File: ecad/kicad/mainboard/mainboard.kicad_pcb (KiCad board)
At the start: 2 copper layers, 99.1 x 81.3 mm, 34 parts, among them IC1 74HC86, J1 SENSORS, J2 CONN_06SILK_FEMALE_PTH, J3 CONN_06SILK_FEMALE_PTH, J4 POWER, J5 SERIAL, M1 Left Motor, M2 Right Motor, U1 Arduino_Nano, U2 TB6612FNG-Module

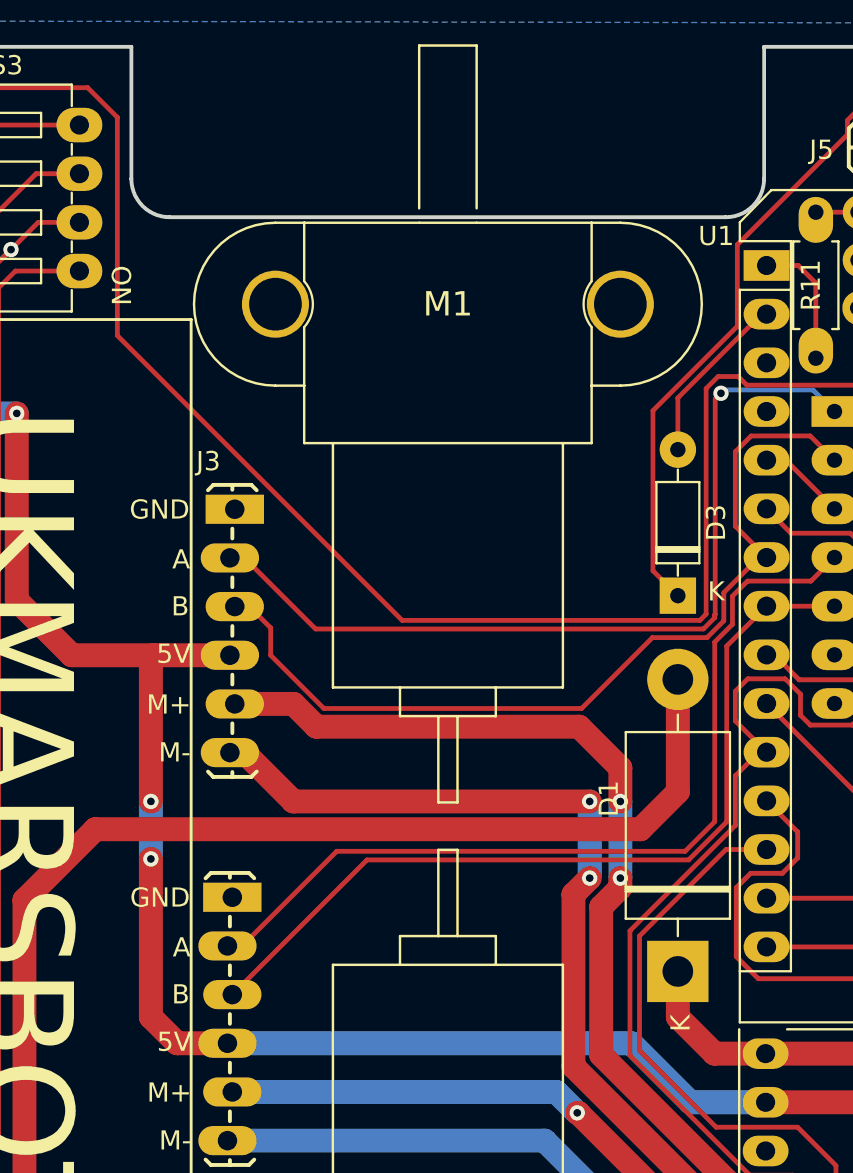
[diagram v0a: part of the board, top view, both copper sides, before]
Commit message: tidy some routes under motors
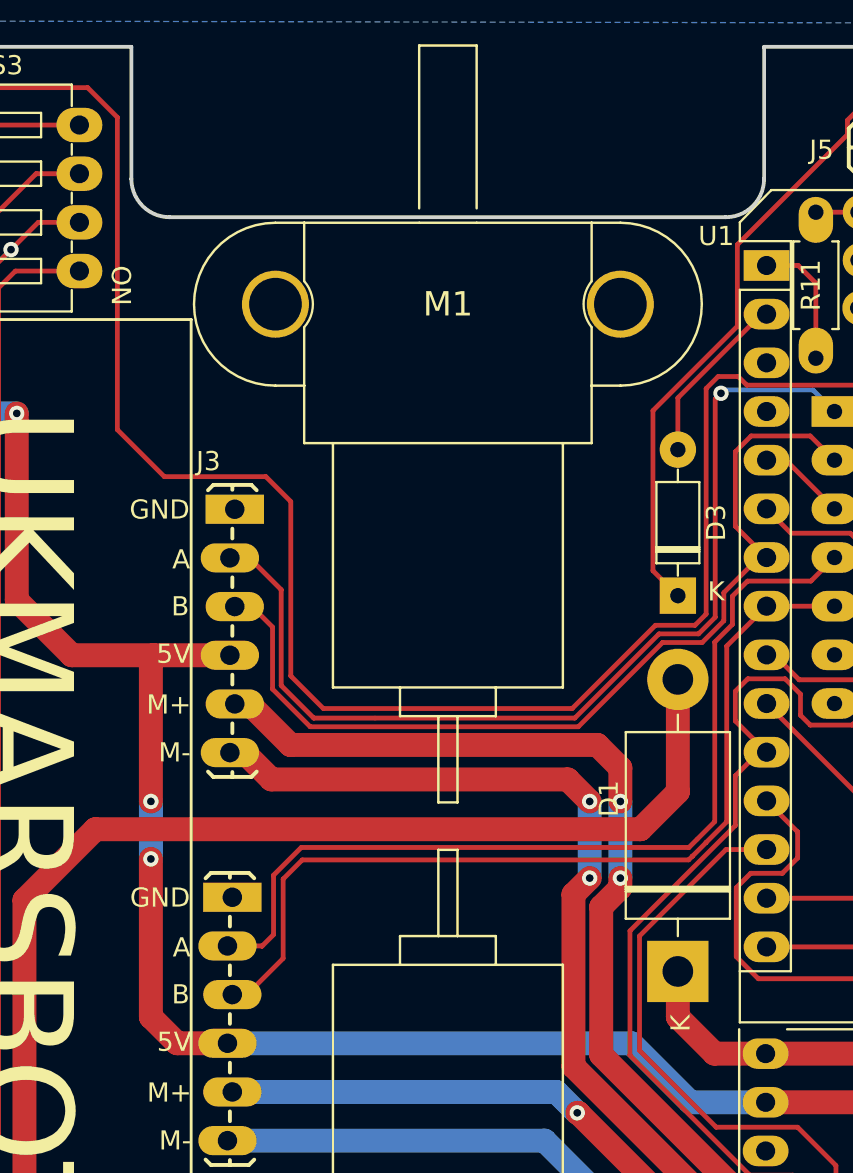
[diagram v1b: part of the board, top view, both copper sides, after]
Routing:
- net /FUNCTION_SELECT: track 123.7 -> 135.7 mm
- net /LEFT_A: track 44.6 -> 52.2 mm
- net /LEFT_B: track 46.0 -> 48.6 mm
- net /RIGHT_A: track 45.7 -> 48.3 mm
- net /RIGHT_B: track 45.2 -> 47.6 mm

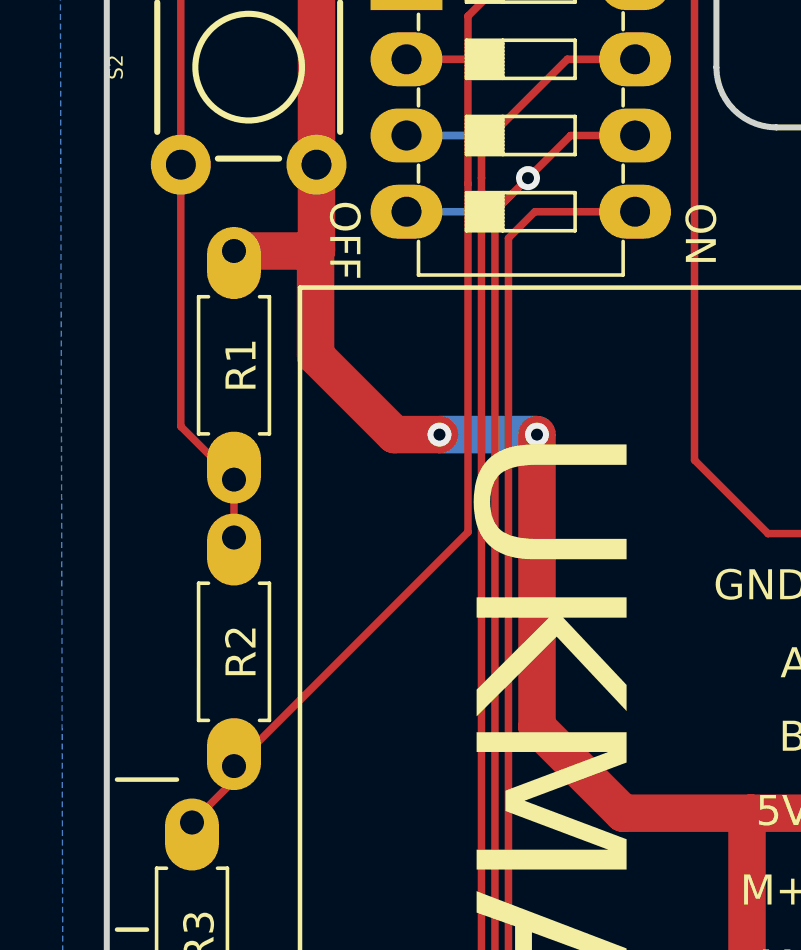
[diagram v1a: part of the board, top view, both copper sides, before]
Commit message: minor change to v1.3 mainboard
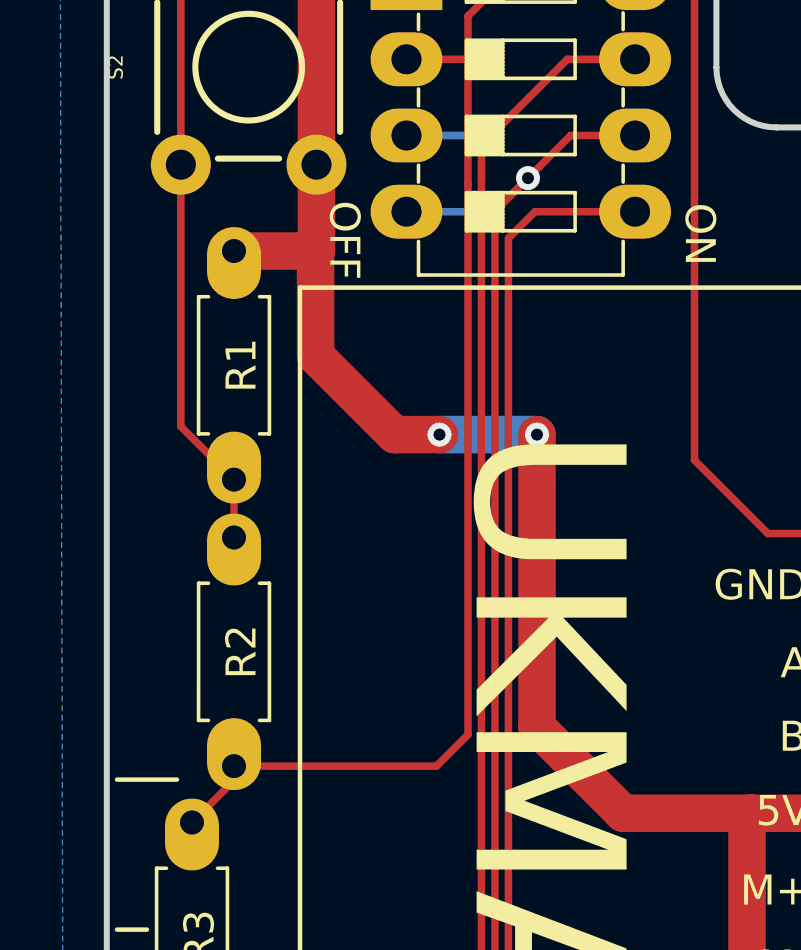
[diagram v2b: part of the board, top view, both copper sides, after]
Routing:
- net Net-(R2-Pad1): track 38.3 -> 42.3 mm
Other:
- board text removed: "V1.3-PJH"
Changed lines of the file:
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@@
   (gr_arc (start 145.500001 88.5) (mid 148.732135 105) (end 145.500001 121.5) (layer "User.9") (width 0.15))
   (gr_arc (start 150.999999 86.5) (mid 154.573865 105) (end 150.999999 123.5) (layer "User.9") (width 0.15))
-  (gr_text "ukmars.org" (at 165 89 90) (layer "B.SilkS")
-    (effects (font (size 2 2) (thickness 0.15)) (justify mirror))
-  )
-  (gr_text "V1.3-PJH" (at 150.5 144.5) (layer "B.SilkS")
-    (effects (font (size 1 1) (thickness 0.15)) (justify mirror))
+  (gr_text "ukmars.org" (at 159.5 72.6 135) (layer "B.SilkS")
+    (effects (font (size 2 2) (thickness 0.4)) (justify mirror))
+  )
+  (gr_text "V1.3a" (at 158.2 138.2 45) (layer "B.SilkS")
+    (effects (font (size 2 2) (thickness 0.4)) (justify mirror))
   )
   (gr_text "UKMARSBOT" (at 157.25 105 90) (layer "B.SilkS")
@@
   (segment (start 117 103.25) (end 117 97.38) (width 1.25) (layer "F.Cu") (net 30))
   (segment (start 78.15 70.99) (end 80.159002 70.99) (width 0.25) (layer "F.Cu") (net 31))
-  (segment (start 80.199501 86.750499) (end 80.199501 75.13802) (width 0.25) (layer "F.Cu") (net 31))
   (segment (start 81.3 68.45) (end 85.77 68.45) (width 0.25) (layer "F.Cu") (net 31))
-  (segment (start 72.4 94.55) (end 80.199501 86.750499) (width 0.25) (layer "F.Cu") (net 31))
+  (segment (start 80.198499 75.137018) (end 80.198499 70.950503) (width 0.25) (layer "F.Cu") (net 31))
+  (segment (start 72.4 94.55) (end 79.15 94.55) (width 0.25) (layer "F.Cu") (net 31))
   (segment (start 80.159002 70.99) (end 80.199501 70.949501) (width 0.25) (layer "F.Cu") (net 31))
   (segment (start 71 96.43) (end 72.4 95.03) (width 0.25) (layer "F.Cu") (net 31))
+  (segment (start 80.198499 70.950503) (end 80.199501 70.949501) (width 0.25) (layer "F.Cu") (net 31))
+  (segment (start 80.199501 93.500499) (end 80.199501 75.13802) (width 0.25) (layer "F.Cu") (net 31))
   (segment (start 80.199501 70.949501) (end 80.199501 69.550499) (width 0.25) (layer "F.Cu") (net 31))
-  (segment (start 80.198499 70.950503) (end 80.199501 70.949501) (width 0.25) (layer "F.Cu") (net 31))
+  (segment (start 79.15 94.55) (end 80.199501 93.500499) (width 0.25) (layer "F.Cu") (net 31))
+  (segment (start 80.199501 69.550499) (end 81.3 68.45) (width 0.25) (layer "F.Cu") (net 31))
   (segment (start 80.199501 75.13802) (end 80.198499 75.137018) (width 0.25) (layer "F.Cu") (net 31))
-  (segment (start 80.199501 69.550499) (end 81.3 68.45) (width 0.25) (layer "F.Cu") (net 31))
-  (segment (start 80.198499 75.137018) (end 80.198499 70.950503) (width 0.25) (layer "F.Cu") (net 31))
   (segment (start 80.649002 100.950998) (end 80.649002 74.950998) (width 0.25) (layer "F.Cu") (net 32))
   (segment (start 80.649002 74.950998) (end 80.65 74.95) (width 0.25) (layer "F.Cu") (net 32))

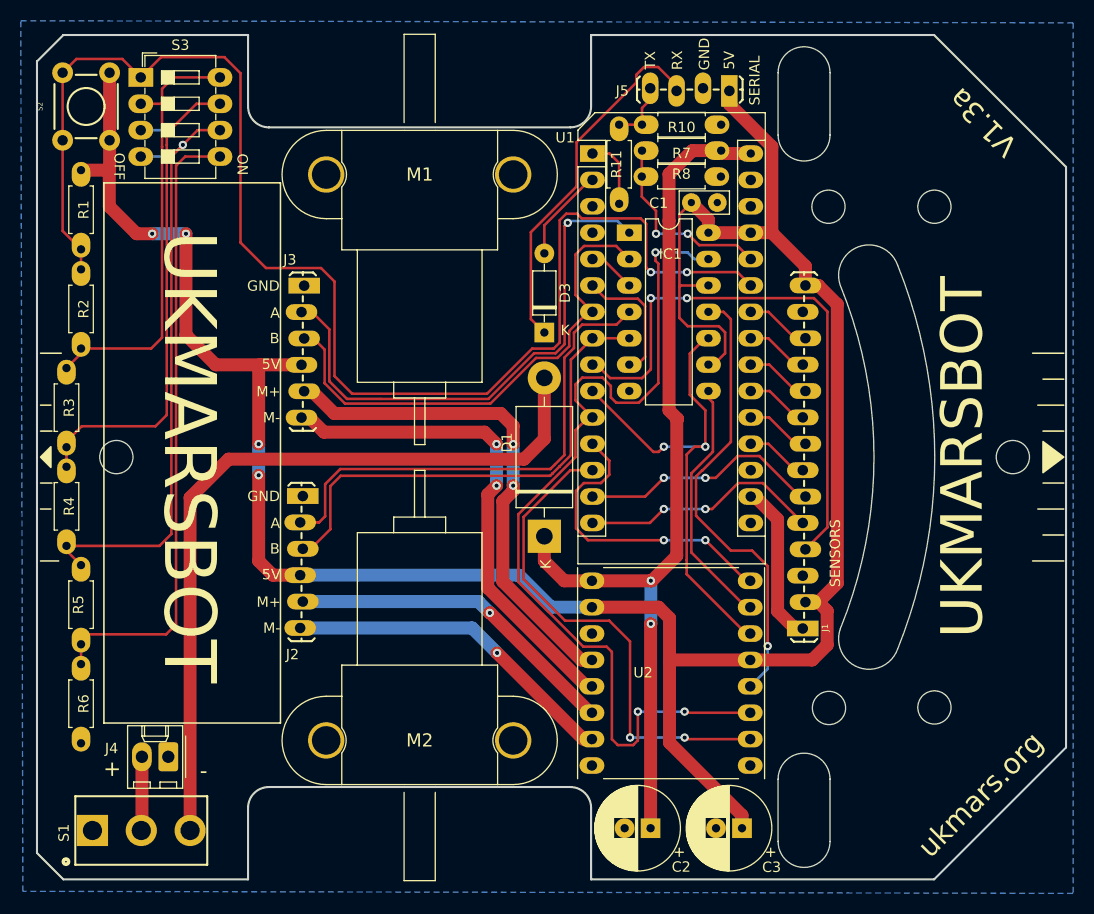
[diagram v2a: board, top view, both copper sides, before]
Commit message: re-route mini wide line sensor
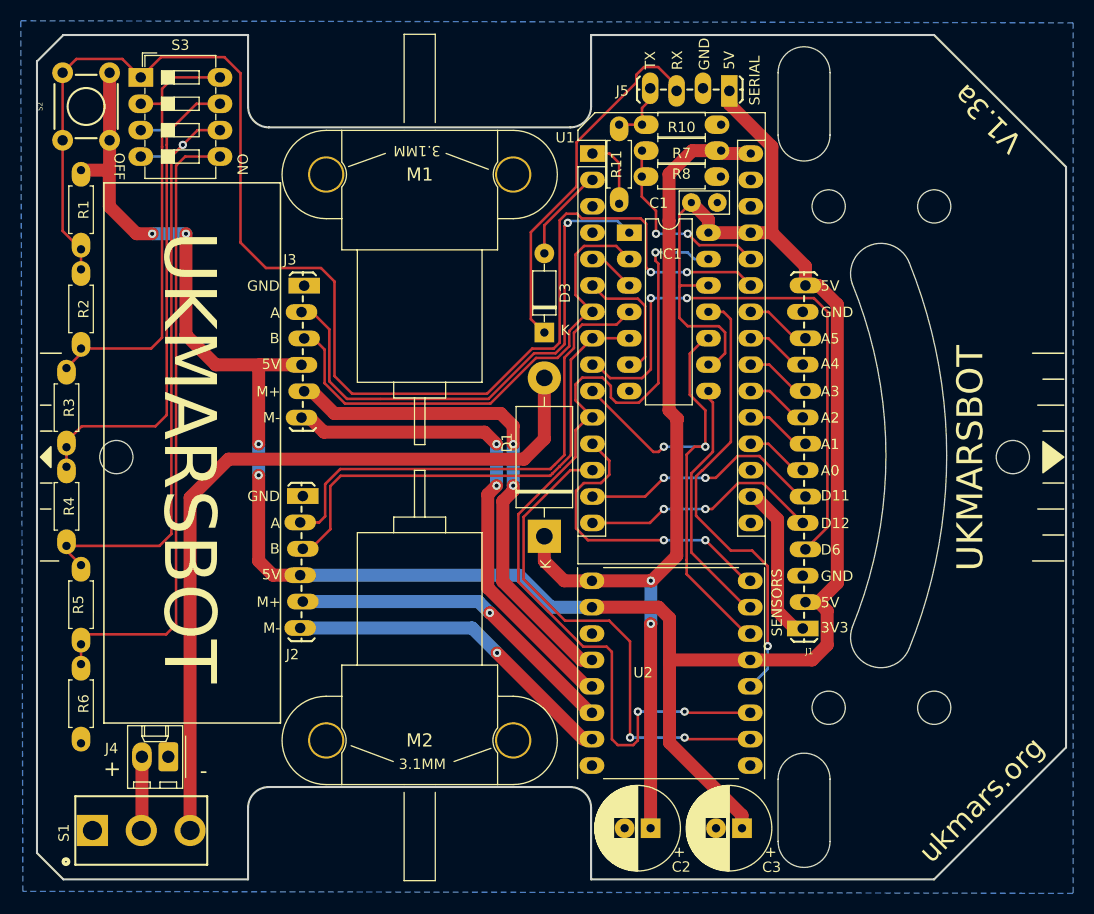
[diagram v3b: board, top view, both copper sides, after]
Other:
- outline, holes or cut-outs redrawn
- board text added: "3V3"
- board text added: "A0"
- board text added: "A1"
- board text added: "A2"
- board text added: "A3"
- board text added: "A4"
- board text added: "A5"
- board text added: "D11"
- board text added: "D12"
- board text added: "D6"

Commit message: updare mounting holes V1.3 mainboard
update V1.3 mainboard mounting holes
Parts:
- H1, H2, H3, H4, H5, H6: footprint MountingHole:MountingHole_3.2mm_M3 -> ukmarsbot:MountingHole_3.2mm_M3_clearance
- moved R3 0.40 mm to (70.6, 104.0)
- moved R4 0.40 mm to (70.6, 113.5)
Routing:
- net Net-(R3-Pad1): track 48.8 -> 47.6 mm
- net Net-(R4-Pad1): track 59.1 -> 59.7 mm

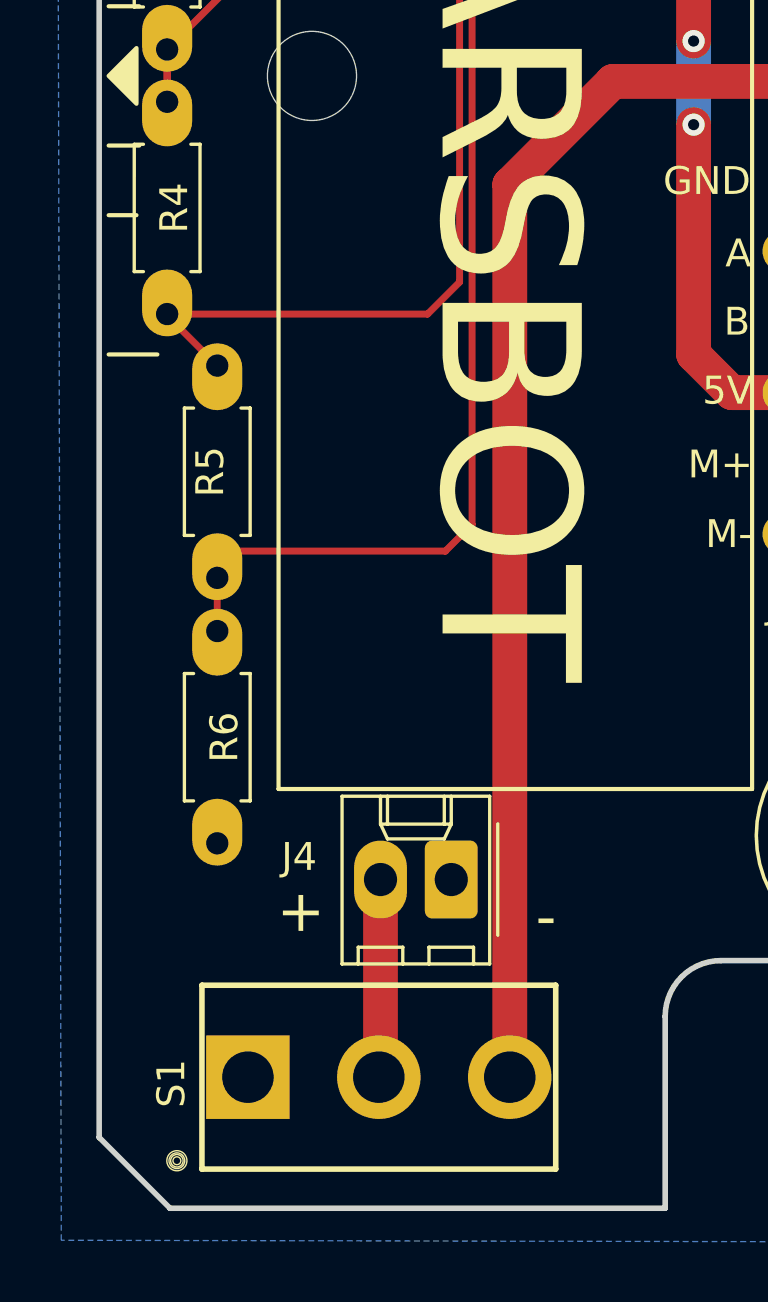
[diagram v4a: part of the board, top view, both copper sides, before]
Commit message: update V1.3 mainboard switches
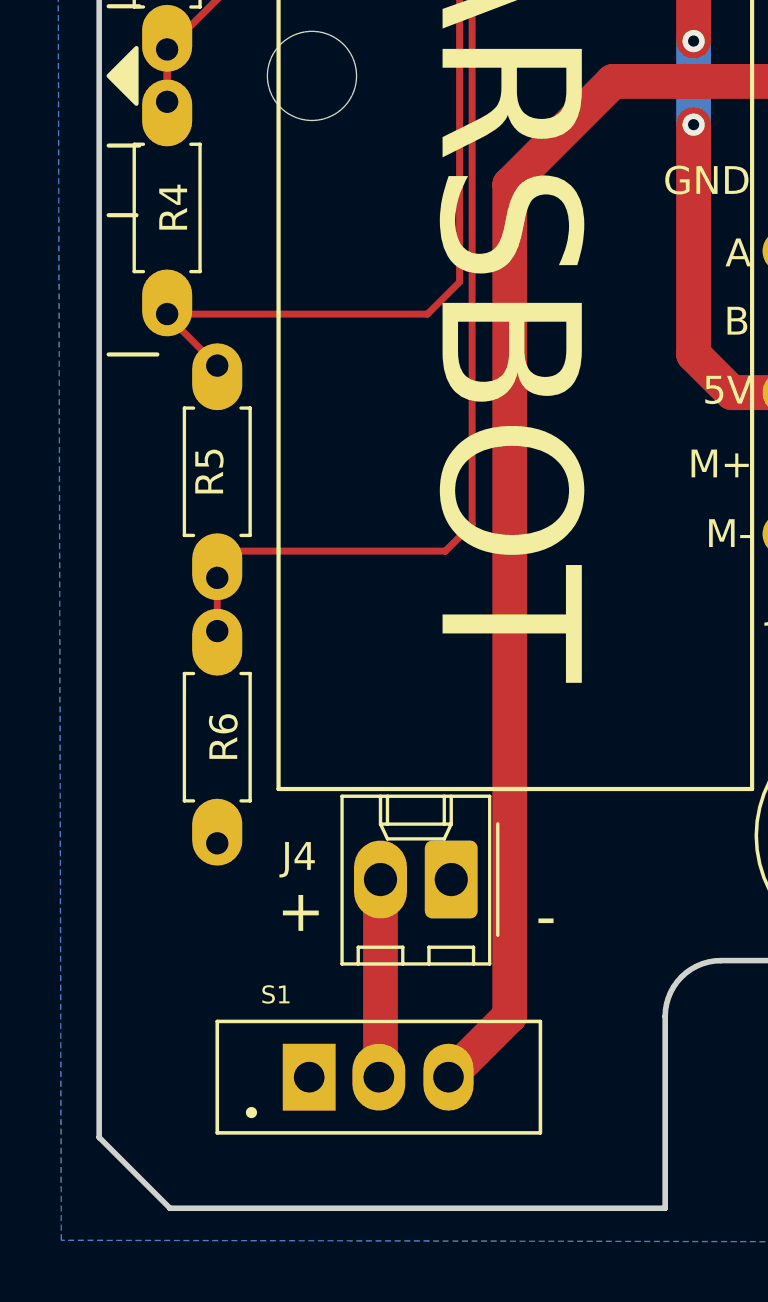
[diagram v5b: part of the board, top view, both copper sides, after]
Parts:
- S1: footprint ukmarsbot:SW_1101M2S3CQE2 -> ukmarsbot:SW_MINI_SPDT_TOGGLE_DAILYWELL_FS1S102M2QES
- turned S1 to 0 degrees
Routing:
- net /SW_PWR: track 74.4 -> 75.3 mm
